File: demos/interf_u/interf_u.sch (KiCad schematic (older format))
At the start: 24 parts, among them P1 DB25FEMELLE, U1 74LS245, U2 74LS688, U3 74LS541, U5 628128, U8 EP600, U9 4003APG120, X1 8MHz

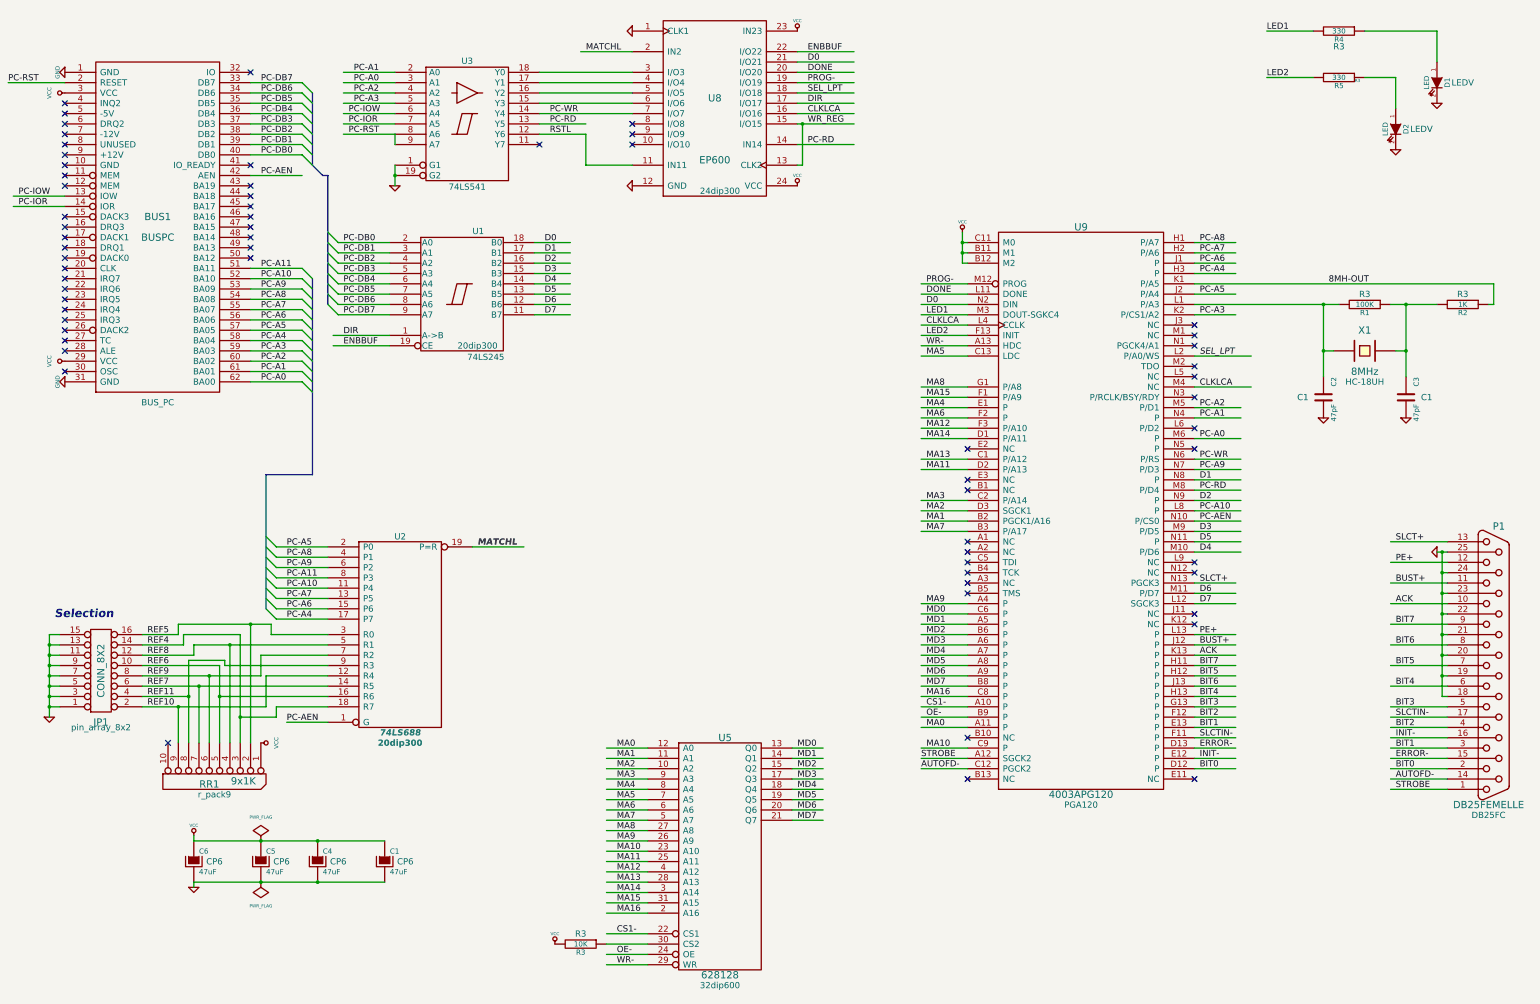
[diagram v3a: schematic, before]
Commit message: Pcbnew: Fix a bug when reading a netlist which forces pcbnew to read lib files to find a footprint even if the right footprint is already loaded (which explains the long time to load netlists) Netlist dialog: add option to report only most important messages. Useful for large boards. class REPORTER: add features to allow a basic message filtering (flags to report all/warning/error messages) Fix Bug #1214599 ( tools are deselected on Move command )
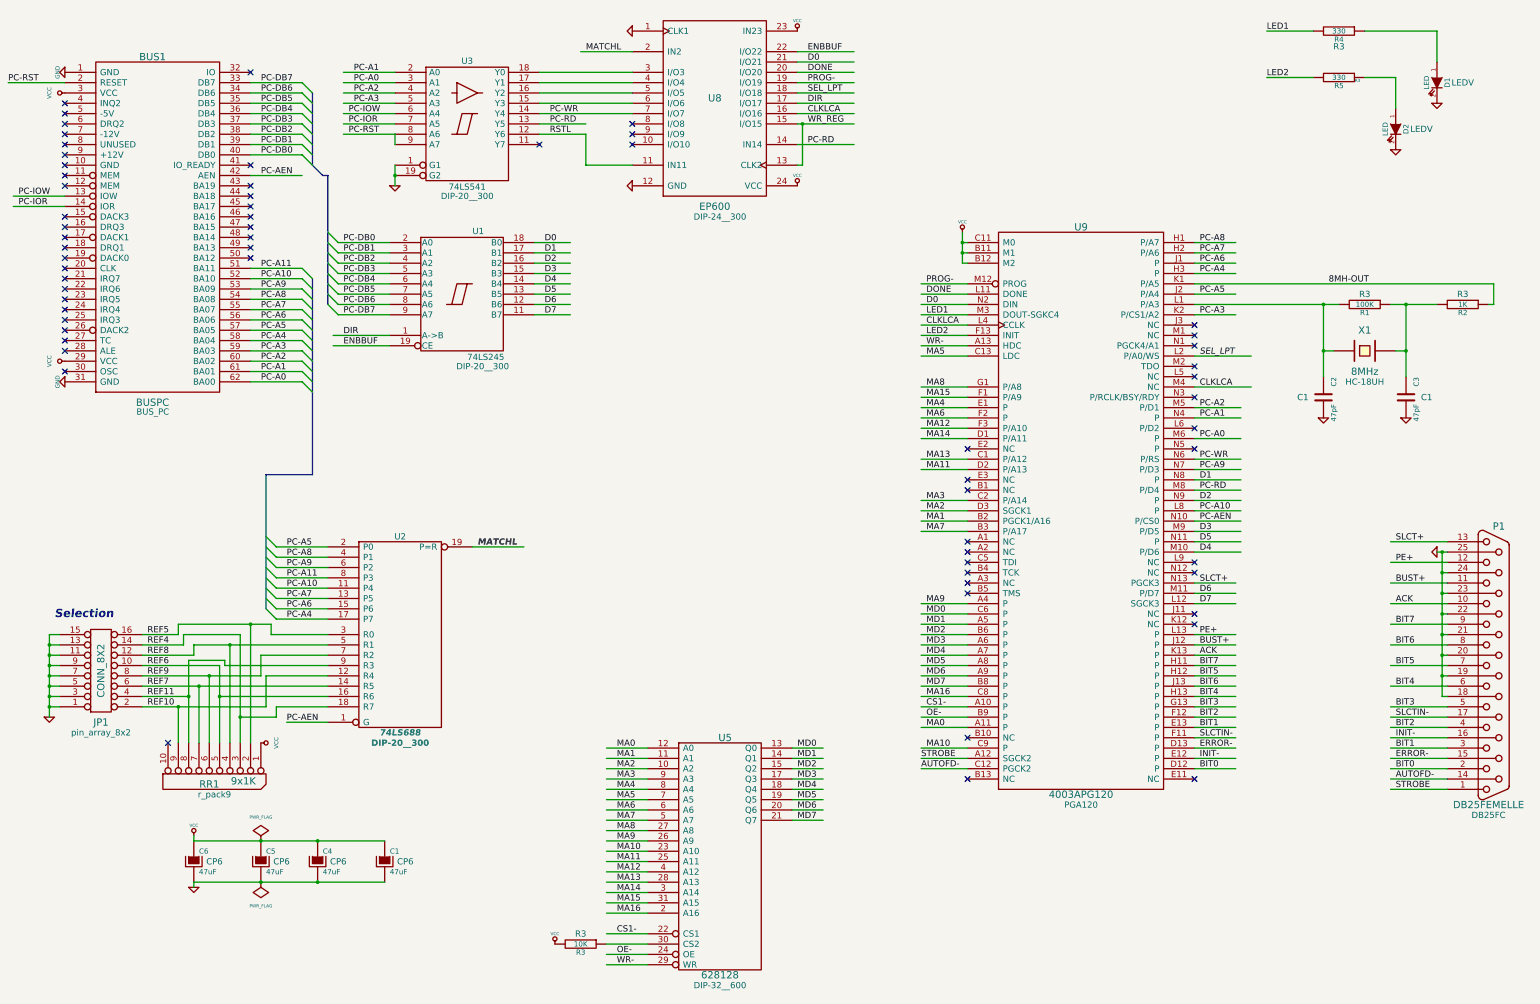
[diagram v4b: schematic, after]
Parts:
- U1, U2: footprint 20dip300 -> DIP-20__300
- U3: footprint (none) -> DIP-20__300
- U5: footprint 32dip600 -> DIP-32__600
- U8: footprint 24dip300 -> DIP-24__300
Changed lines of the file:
@@
 $EndDescr
 $Bitmap
-Pos 9250 10500
+Pos 9350 10600
 Scale 1,000000
 Data
@@
 A2 94 8E 79 E6 79 49 E6 FD 75 9E B9 C4 BC BF CE 33 97 98 F7 D7 79 E6 12 F3 FE 3A CF 5C E2 E7 E2
 03 93 93 93 FD BA 8E 79 E6 39 19 8E FB EB DC 15 0B E6 F9 D5 61 7E 3F 30 CF 5C 62 DE 5F E7 99 4B
-FC 1F 94 BD 62 D3 EE A5 8B 6B 00 00 00 00 49 45 4E 44 AE 42 60 82 11
+FC 1F 94 BD 62 D3 EE A5 8B 6B 00 00 00 00 49 45 4E 44 AE 42 60 82 10
 EndData
 $EndBitmap
@@
 F 0 "U3" H 5250 2525 60  0000 C BNN
 F 1 "74LS541" H 5250 1375 60  0000 C TNN
-F 2 "" H 5250 1950 60  0001 C CNN
+F 2 "DIP-20__300" H 5250 1250 60  0000 C CNN
 F 3 "" H 5250 1950 60  0001 C CNN
 	1    5250 1950
@@
 F 0 "JP1" H 1700 7750 70  0000 C CNN
 F 1 "CONN_8X2" V 1700 7250 70  0000 C CNN
-F 2 "pin_array_8x2" H 1700 7800 60  0000 C CNN
+F 2 "pin_array_8x2" H 1700 7850 60  0000 C CNN
 F 3 "" H 1700 7250 60  0001 C CNN
 	1    1700 7250
@@
 F 0 "U5" H 7750 10200 70  0000 C CNN
 F 1 "628128" H 7700 7900 70  0000 C CNN
-F 2 "32dip600" H 7700 7800 60  0000 C CNN
+F 2 "DIP-32__600" H 7700 7800 60  0000 C CNN
 F 3 "" H 7700 9050 60  0001 C CNN
 	1    7700 9050
@@
 F 0 "U2" H 4600 7850 60  0000 C CNN
 F 1 "74LS688" H 4600 5950 60  0000 C CIB
-F 2 "20dip300" H 4600 5850 60  0000 C CNB
+F 2 "DIP-20__300" H 4600 5850 60  0000 C CNB
 F 3 "" H 4600 6900 60  0001 C CNN
 	1    4600 6900
@@
 P 7650 1800
 F 0 "U8" H 7650 1900 70  0000 C CNN
-F 1 "EP600" H 7650 1300 70  0000 C CNN
-F 2 "24dip300" H 7700 1000 60  0000 C CNN
+F 1 "EP600" H 7650 850 70  0000 C CNN
+F 2 "DIP-24__300" H 7700 750 60  0000 C CNN
 F 3 "" H 7650 1800 60  0001 C CNN
 	1    7650 1800
@@
 F 0 "U1" H 5300 4175 60  0000 L BNN
 F 1 "74LS245" H 5250 3025 60  0000 L TNN
-F 2 "20dip300" H 5350 3100 60  0000 C CNN
+F 2 "DIP-20__300" H 5400 2900 60  0000 C CNN
 F 3 "" H 5200 3600 60  0001 C CNN
 	1    5200 3600
@@
 U 1 1 322D3011
 P 2250 2950
-F 0 "BUS1" H 2250 3050 70  0000 C CNN
-F 1 "BUSPC" H 2250 2850 70  0000 C CNN
-F 2 "BUS_PC" H 2250 1250 60  0000 C CNN
+F 0 "BUS1" H 2200 4600 70  0000 C CNN
+F 1 "BUSPC" H 2200 1250 70  0000 C CNN
+F 2 "BUS_PC" H 2202 1160 60  0000 C CNN
 F 3 "" H 2250 2950 60  0001 C CNN
 	1    2250 2950

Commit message: Minor fixes: specctra export: skip malformed circles (having a radius = 0)  in board outline creation, which can crash 3d-viewer or vrml export. dialog_fp_lib_table: remember during a session the last open table (global or local). drawing_tool: fix compil warning Update demos.
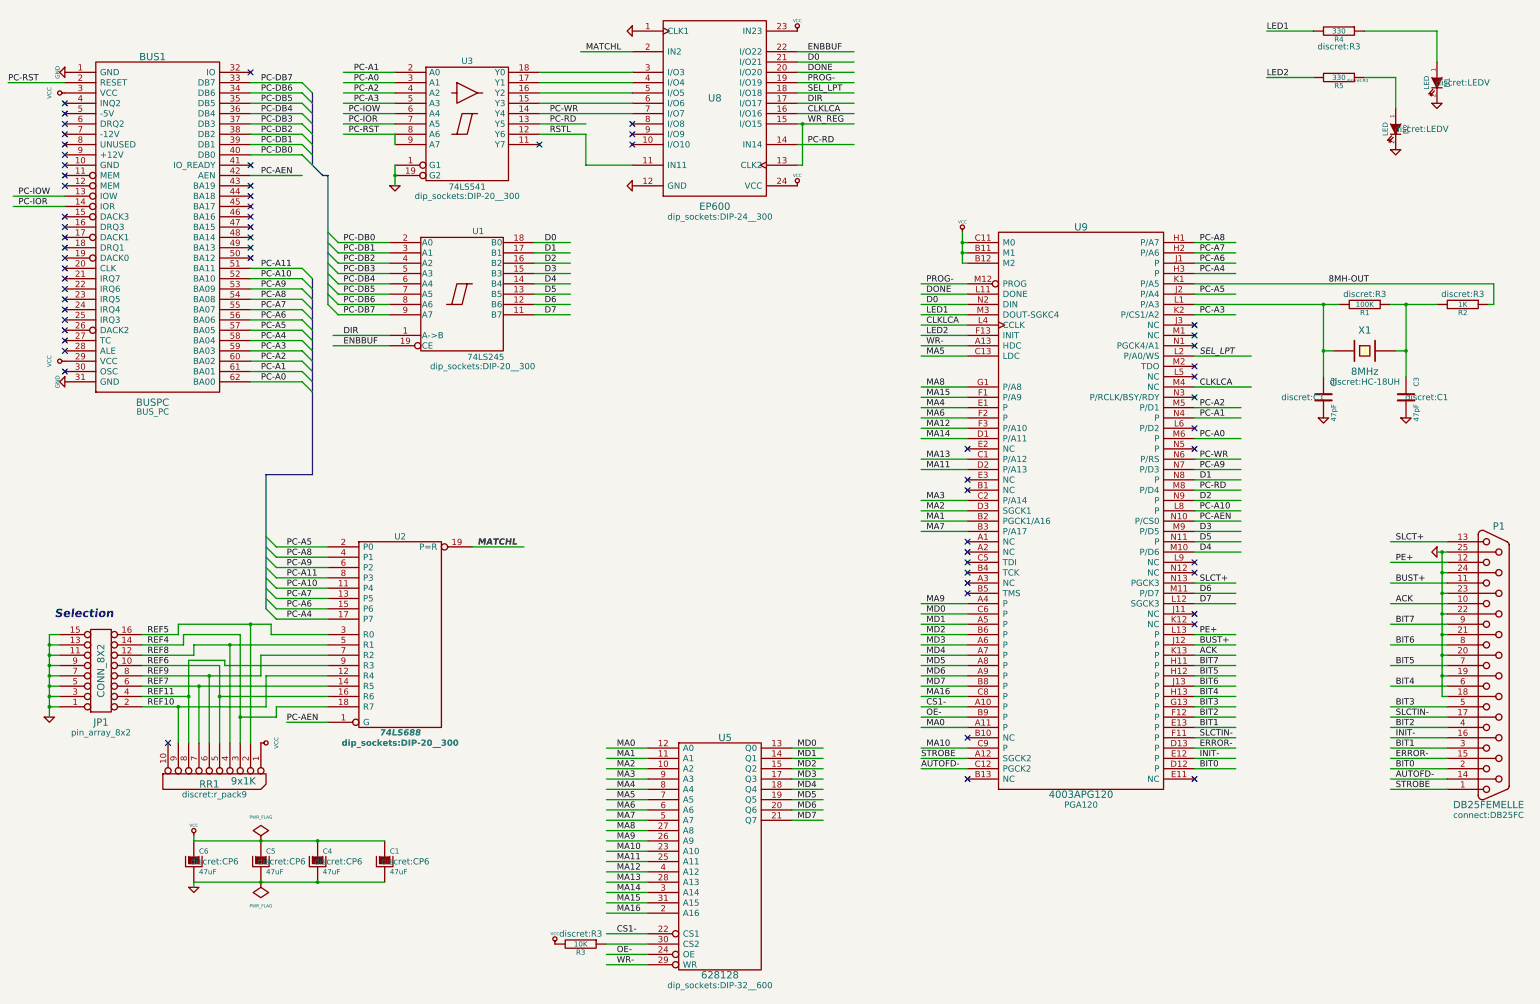
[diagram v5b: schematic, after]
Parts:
- C1, C4, C5, C6: footprint CP6 -> discret:CP6
- C2, C3: footprint C1 -> discret:C1
- D1, D2: footprint LEDV -> discret:LEDV
- P1: footprint DB25FC -> connect:DB25FC
- R1, R2, R3, R4, R5: footprint R3 -> discret:R3
- RR1: footprint r_pack9 -> discret:r_pack9
- U1, U2, U3: footprint DIP-20__300 -> dip_sockets:DIP-20__300
- U5: footprint DIP-32__600 -> dip_sockets:DIP-32__600
- U8: footprint DIP-24__300 -> dip_sockets:DIP-24__300
- X1: footprint HC-18UH -> discret:HC-18UH
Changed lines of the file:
@@
 A2 94 8E 79 E6 79 49 E6 FD 75 9E B9 C4 BC BF CE 33 97 98 F7 D7 79 E6 12 F3 FE 3A CF 5C E2 E7 E2
 03 93 93 93 FD BA 8E 79 E6 39 19 8E FB EB DC 15 0B E6 F9 D5 61 7E 3F 30 CF 5C 62 DE 5F E7 99 4B
-FC 1F 94 BD 62 D3 EE A5 8B 6B 00 00 00 00 49 45 4E 44 AE 42 60 82 10
+FC 1F 94 BD 62 D3 EE A5 8B 6B 00 00 00 00 49 45 4E 44 AE 42 60 82 41
 EndData
 $EndBitmap
@@
 	3900 6900 3350 6900
 Wire Wire Line
-	3350 6800 3350 6900
+	3350 6900 3350 6800
 Wire Wire Line
 	3350 6800 2450 6800
@@
 	2500 7000 2500 6900
 Wire Wire Line
-	3050 6900 2500 6900
-Wire Wire Line
-	3050 7950 3050 6900
+	2500 6900 3050 6900
+Wire Wire Line
+	3050 6900 3050 7950
 Wire Wire Line
 	3900 7600 3400 7600
@@
 	3750 3450 3750 5350
 Wire Bus Line
-	3300 5350 3750 5350
+	3750 5350 3300 5350
 Wire Bus Line
-	3300 6650 3300 5350
+	3300 5350 3300 6650
 Wire Bus Line
 	3900 3700 3900 2450
@@
 F 0 "U3" H 5250 2525 60  0000 C BNN
 F 1 "74LS541" H 5250 1375 60  0000 C TNN
-F 2 "DIP-20__300" H 5250 1250 60  0000 C CNN
+F 2 "dip_sockets:DIP-20__300" H 5250 1250 60  0000 C CNN
 F 3 "" H 5250 1950 60  0001 C CNN
 	1    5250 1950
@@
 F 0 "RR1" V 2800 8300 70  0000 C CNN
 F 1 "9x1K" V 2770 8630 70  0000 C CNN
-F 2 "r_pack9" V 2900 8350 60  0000 C CNN
+F 2 "discret:r_pack9" V 2900 8350 60  0000 C CNN
 F 3 "" H 2750 8300 60  0001 C CNN
 	1    2750 8300
@@
 F 0 "P1" H 15250 8550 70  0000 C CNN
 F 1 "DB25FEMELLE" H 15150 5850 70  0000 C CNN
-F 2 "DB25FC" H 15150 5750 60  0000 C CNN
+F 2 "connect:DB25FC" H 15150 5750 60  0000 C CNN
 F 3 "" H 15200 7200 60  0001 C CNN
 	1    15200 7200
@@
 F 0 "R3" V 6430 9900 50  0000 C CNN
 F 1 "10K" V 6350 9900 50  0000 C CNN
-F 2 "R3" V 6250 9900 60  0000 C CNN
+F 2 "discret:R3" V 6250 9900 60  0000 C CNN
 F 3 "" H 6350 9900 60  0001 C CNN
 	1    6350 9900
@@
 F 0 "U5" H 7750 10200 70  0000 C CNN
 F 1 "628128" H 7700 7900 70  0000 C CNN
-F 2 "DIP-32__600" H 7700 7800 60  0000 C CNN
+F 2 "dip_sockets:DIP-32__600" H 7700 7800 60  0000 C CNN
 F 3 "" H 7700 9050 60  0001 C CNN
 	1    7700 9050
@@
 F 0 "C3" V 14450 4750 50  0000 C CNN
 F 1 "47pF" V 14450 4450 50  0000 C CNN
-F 2 "C1" H 14550 4600 60  0000 C CNN
+F 2 "discret:C1" H 14550 4600 60  0000 C CNN
 F 3 "" H 14350 4600 60  0001 C CNN
 	1    14350 4600
@@
 F 0 "C2" V 13650 4750 50  0000 C CNN
 F 1 "47pF" V 13650 4450 50  0000 C CNN
-F 2 "C1" H 13350 4600 60  0000 C CNN
+F 2 "discret:C1" H 13350 4600 60  0000 C CNN
 F 3 "" H 13550 4600 60  0001 C CNN
 	1    13550 4600
@@
 F 0 "X1" H 13950 4350 70  0000 C CNN
 F 1 "8MHz" H 13950 3950 70  0000 C CNN
-F 2 "HC-18UH" H 13950 3850 60  0000 C CNN
+F 2 "discret:HC-18UH" H 13950 3850 60  0000 C CNN
 F 3 "" H 13950 4150 60  0001 C CNN
 	1    13950 4150
@@
 F 0 "R2" V 14980 3700 50  0000 C CNN
 F 1 "1K" V 14900 3700 50  0000 C CNN
-F 2 "R3" V 14800 3700 60  0000 C CNN
+F 2 "discret:R3" V 14800 3700 60  0000 C CNN
 F 3 "" H 14900 3700 60  0001 C CNN
 	1    14900 3700
@@
 F 0 "R1" V 14030 3700 50  0000 C CNN
 F 1 "100K" V 13950 3700 50  0000 C CNN
-F 2 "R3" V 13850 3700 60  0000 C CNN
+F 2 "discret:R3" V 13850 3700 60  0000 C CNN
 F 3 "" H 13950 3700 60  0001 C CNN
 	1    13950 3700
@@
 F 0 "C1" H 4500 9200 50  0000 L CNN
 F 1 "47uF" H 4500 9000 50  0000 L CNN
-F 2 "CP6" H 4650 9100 60  0000 C CNN
+F 2 "discret:CP6" H 4650 9100 60  0000 C CNN
 F 3 "" H 4450 9100 60  0001 C CNN
 	1    4450 9100
@@
 F 0 "C4" H 3850 9200 50  0000 L CNN
 F 1 "47uF" H 3850 9000 50  0000 L CNN
-F 2 "CP6" H 4000 9100 60  0000 C CNN
+F 2 "discret:CP6" H 4000 9100 60  0000 C CNN
 F 3 "" H 3800 9100 60  0001 C CNN
 	1    3800 9100
@@
 F 0 "C5" H 3300 9200 50  0000 L CNN
 F 1 "47uF" H 3300 9000 50  0000 L CNN
-F 2 "CP6" H 3450 9100 60  0000 C CNN
+F 2 "discret:CP6" H 3450 9100 60  0000 C CNN
 F 3 "" H 3250 9100 60  0001 C CNN
 	1    3250 9100
@@
 F 0 "C6" H 2650 9200 50  0000 L CNN
 F 1 "47uF" H 2650 9000 50  0000 L CNN
-F 2 "CP6" H 2800 9100 60  0000 C CNN
+F 2 "discret:CP6" H 2800 9100 60  0000 C CNN
 F 3 "" H 2600 9100 60  0001 C CNN
 	1    2600 9100
@@
 F 0 "U2" H 4600 7850 60  0000 C CNN
 F 1 "74LS688" H 4600 5950 60  0000 C CIB
-F 2 "DIP-20__300" H 4600 5850 60  0000 C CNB
+F 2 "dip_sockets:DIP-20__300" H 4600 5850 60  0000 C CNB
 F 3 "" H 4600 6900 60  0001 C CNN
 	1    4600 6900
@@
 F 0 "D2" H 14250 2100 50  0000 C CNN
 F 1 "LED" H 14250 1900 50  0000 C CNN
-F 2 "LEDV" V 14250 2250 60  0000 C CNN
+F 2 "discret:LEDV" V 14250 2250 60  0000 C CNN
 F 3 "" H 14250 2000 60  0001 C CNN
 	1    14250 2000
@@
 F 0 "D1" H 14650 1650 50  0000 C CNN
 F 1 "LED" H 14650 1450 50  0000 C CNN
-F 2 "LEDV" V 14650 1800 60  0000 C CNN
+F 2 "discret:LEDV" V 14650 1800 60  0000 C CNN
 F 3 "" H 14650 1550 60  0001 C CNN
 	1    14650 1550
@@
 F 0 "R5" V 13780 1500 50  0000 C CNN
 F 1 "330" V 13700 1500 50  0000 C CNN
-F 2 "R3" V 13730 1680 30  0000 C CNN
+F 2 "discret:R3" V 13730 1680 30  0000 C CNN
 F 3 "" H 13700 1500 60  0001 C CNN
 	1    13700 1500
@@
 F 0 "R4" V 13780 1050 50  0000 C CNN
 F 1 "330" V 13700 1050 50  0000 C CNN
-F 2 "R3" V 13850 1050 60  0000 C CNN
+F 2 "discret:R3" V 13850 1050 60  0000 C CNN
 F 3 "" H 13700 1050 60  0001 C CNN
 	1    13700 1050
@@
 F 0 "U8" H 7650 1900 70  0000 C CNN
 F 1 "EP600" H 7650 850 70  0000 C CNN
-F 2 "DIP-24__300" H 7700 750 60  0000 C CNN
+F 2 "dip_sockets:DIP-24__300" H 7700 750 60  0000 C CNN
 F 3 "" H 7650 1800 60  0001 C CNN
 	1    7650 1800
@@
 F 0 "U1" H 5300 4175 60  0000 L BNN
 F 1 "74LS245" H 5250 3025 60  0000 L TNN
-F 2 "DIP-20__300" H 5400 2900 60  0000 C CNN
+F 2 "dip_sockets:DIP-20__300" H 5400 2900 60  0000 C CNN
 F 3 "" H 5200 3600 60  0001 C CNN
 	1    5200 3600

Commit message: demos/ schematic tidying
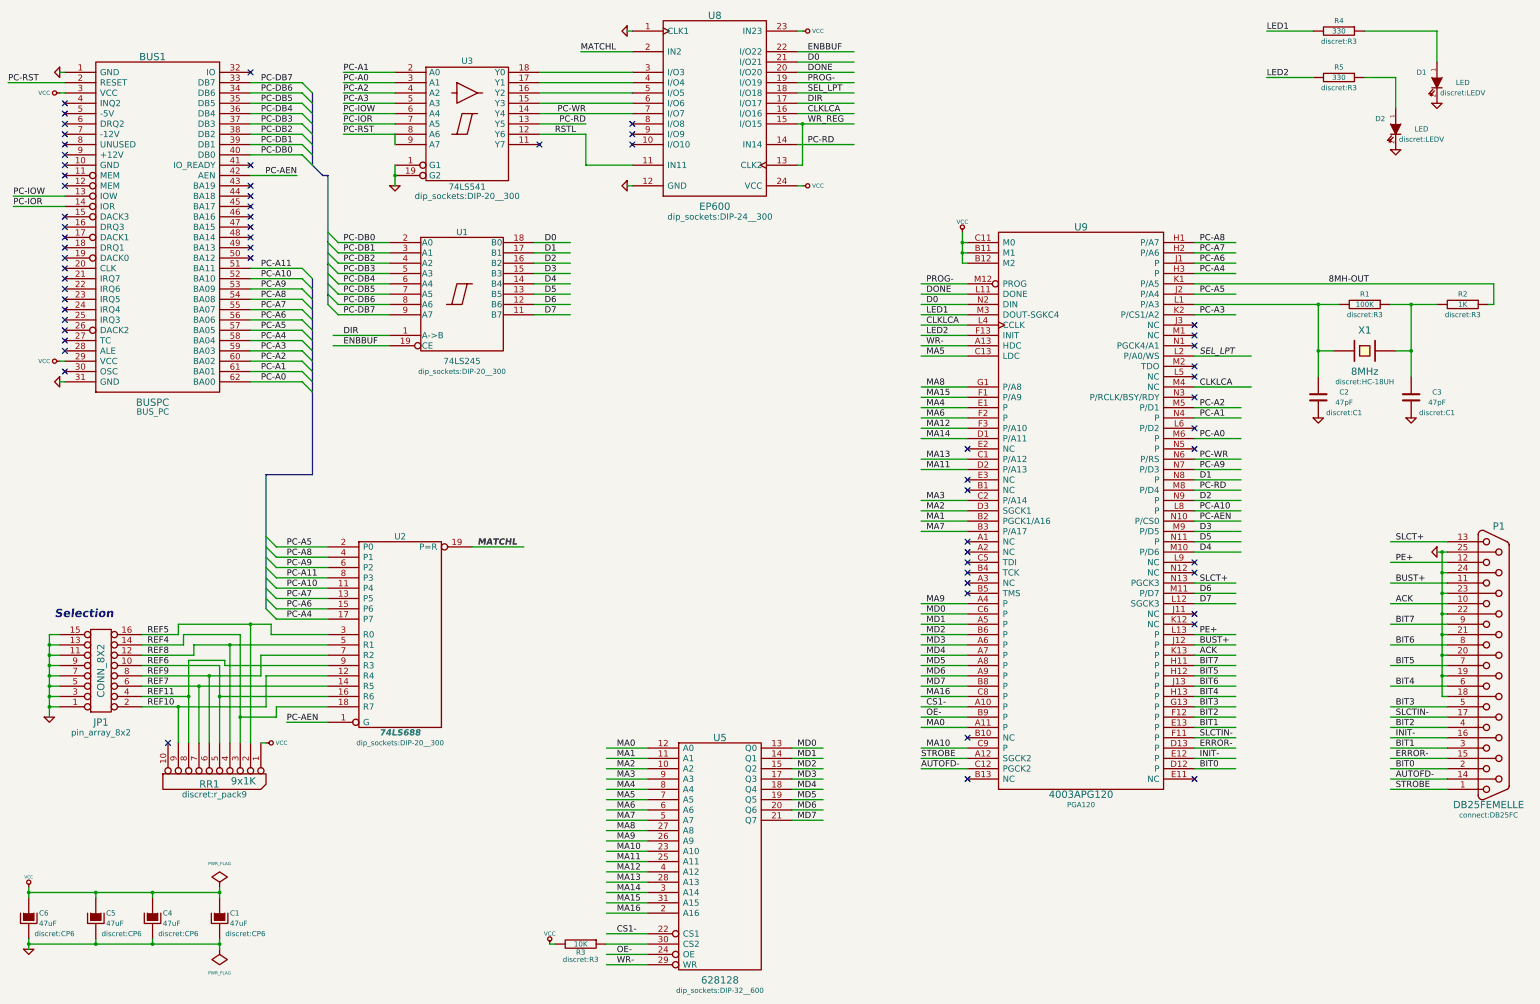
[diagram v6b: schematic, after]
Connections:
- wire segments 278 -> 294
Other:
- moved on the sheet: C1, C2, C3, C4, C5, C6
